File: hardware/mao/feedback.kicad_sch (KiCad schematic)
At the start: 20 parts, among them J501 LRA, Q501 AO3400A, U501 MAX98357AETE+T, U502 DRV2605LDGSR, U503 IRM-H638T/TR2

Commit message: MAO A0 revision: stock Winstar panel through a tail slot, AW9364 backlight, routed 4-layer board
Hardware changes from the verification audits:
- display: stock Winstar WF0128BTYAA4DNN0 (70 mm tail) through a routed slot at 9 o'clock
  to J301 on B.Cu; panel pin k on pad 19-k
- backlight: VLED+ on VSYS into an AW9364 (U303) constant-current sink, 40 mA nominal;
  Q301/R303-R305 removed
- display rail: TPS22919 (SC70-6, 1.1 mm: fits under the panel) with its VIN cap; CT cap gone
- +3V3 at 3.18 V (FB 536k), UVLO filter cap, charger ISET 4.3k (207 mA), /CE from the
  expander with a pull-down, charger moved to F under the panel, SD_MODE series 2.2k
- IR_TX on GPIO38, EXP_RST_N on GPIO39 (MTCK reset pull-up lit the IR LEDs)
- IR receiver and ToF pulled inside the ring lip; M2 boss / screw-head keep-outs

Layout: re-placed and re-routed. DRC 0 violations, 0 unconnected; every plane one piece
(the grid router now undoes any L3 route or via that splits a plane); 192 through vias.
Silk: type scale, 6 x 6 S/N field with the JLC order-number placeholder, 4.6 mm back mark,
references kept off vias, and a few easter eggs (a sleeping cat under the face, boop,
meow, 9 lives, MADE FOR BAD IDEAS).

Checks: ERC 0, silk text 0 findings, enclosure check 0 findings (mech_check.py), all
simulations pass (S3 AW9364, S10 TPS22919, S13 207 mA). Docs: bring-up, factory test,
power budget, architecture, mechanical (tail path), pin map. Firmware: dev command
"mao power charge off|on", self-test pad floor for the 3.18 V rail; merge patch regenerated.

Co-Authored-By: Claude Opus 5.5 <noreply@anthropic.com>
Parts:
- added R507: 2.2k, Resistor_SMD:R_0402_1005Metric, symbol Device:R
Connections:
- net AMP_SD_N: now also R507.1; no longer U501.4 (~{SD_MODE})
- new net AMP_SD: R507.2, U501.4 (~{SD_MODE})
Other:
- note added: "(117)."
- note added: "(datasheet state, deliberate). Speaker:"
- note added: "(datasheet: series R when VDDIO can"
- note added: "MAX98357A I2S class-D from VSYS. SD_MODE"
- note added: "MAX98357A I2S class-D from VSYS. SD_MODE from the expander through 2.2k (datasheet: series R when VDDIO can exceed"
- note added: "Same Sky CMS-150803-088S-X8 (15 x 8 x 3"
- note added: "Sky CMS-150803-088S-X8 (15 x 8 x 3 mm, 8 ohm, 0.8 W) in the base at 9 o'clock; its own spring contacts press on two"
- note added: "V = left channel. GAIN_SLOT open = 9 dB"
- note added: "VDD): low = 0.6 uA shutdown, 3.2 V = left channel. GAIN_SLOT open = 9 dB (datasheet state, deliberate). Speaker: Same"
- note added: "exceed VDD): low = 0.6 uA shutdown, 3.2"
- note added: "from the expander through 2.2k"
- note added: "mm, 8 ohm, 0.8 W) in the base at 9"
- note added: "o'clock; its own spring contacts press"
- note added: "on two pads on B.Cu (LS501)."
- note added: "pads on B.Cu (LS501)."
- note added: "rating at any VSYS up to 4.5 V and any Vf). AO3400A low side, gate pulled down and driven from GPIO38, a pin without a reset pull-up: dark at reset"
- note removed: "9 o'clock; its own spring contacts press on two pads on B.Cu (LS501)."
- note removed: "= 9 dB (datasheet state, deliberate). Speaker: Same Sky CMS-150803-088S-X8 (15 x 8 x 3 mm, 8 ohm, 0.8 W) in the base at"
- note removed: "MAX98357A I2S class-D from VSYS. SD_MODE from the expander: low = 0.6 uA shutdown, 3.3 V = left channel. GAIN_SLOT open"
- note removed: "rating at any VSYS up to 4.5 V and any Vf). AO3400A low side, gate pulled down: dark at reset (117)."
- moved on the sheet: C506, R505, R506, U503

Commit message: MAO A0 schematic: one frame per block, wired local nets, no overprinted names
ODD JOBS audit 2, X8 (rules 187, 188):
- Parts added late (C111, R117, R507) join their block's frame instead of opening a duplicate frame
  with a copy of its note that ran over the neighbours.
- A two-pin part on a net that only joins it to one side pin of its block's IC is wired to that pin
  (the pin's label still names the net, so board, rules and procedures keep their names); feedback and
  UVLO-style dividers hang off their pin as a divider column. Columns step so no wire crosses a part.
- Adjacent pins on one rail share one rail symbol, joined by a wire; a sideways rail symbol keeps its
  name on its own row; turned passives, LEDs and diodes keep their reference and value off the body.
- Rail-source declarations sit in their own frame in the layout flow, not over the title block.
- Two stale notes corrected (C105 distance to VIN, R204 A0 voltage); board fields synced.

ERC 0, DRC 0 / 0 / parity 0.

Co-Authored-By: Claude Opus 5.5 <noreply@anthropic.com>
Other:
- note added: "3.2 V = left channel. GAIN_SLOT open = 9 dB (datasheet state, deliberate). Speaker: Same Sky CMS-150803-088S-X8 (15 x 8 x 3 mm, 8 ohm, 0.8 W) in"
- note added: "65 mA rating at any VSYS up to 4.5 V and any Vf). AO3400A low side, gate pulled down and driven from GPIO38, a pin without a reset"
- note added: "DRV2605L closed-loop LRA driver from VSYS, I2C 0x5A, EN from the expander (4 uA off). IN/TRIG low: playback by"
- note added: "I2C. Pin 6 VDD/NC left open (SLOS854D: optional supply, tie to VDD or float). LRA LD0832AA (235 Hz, 1.8 Vrms)"
- note added: "IRM-H638T (as LCDkit), top-view, looking up through the window border. Powered from expander"
- note added: "MAX98357A I2S class-D from VSYS. SD_MODE from the expander through 2.2k (datasheet: series R when VDDIO can exceed VDD): low = 0.6 uA shutdown,"
- note added: "P5 through 100R/4.7 uF only when listening (0.4 mA). OUT pull-up goes to the switched"
- note added: "RAIL SOURCES"
- note added: "Two side-emitting 940 nm LEDs at the back edge (B.Cu), each with its own 56R from VSYS (26-59 mA pulses at 38 kHz, 33 % duty: under the"
- note added: "defined low while it is off."
- note added: "glued to the base, leads to J501."
- note added: "pull-up: dark at reset (117)."
- note added: "supply, never to +3V3, so an unpowered receiver is never back-powered and GPIO40 reads a"
- note added: "the base at 9 o'clock; its own spring contacts press on two pads on B.Cu (LS501)."
- note removed: "(117)."
- note removed: "(datasheet state, deliberate). Speaker:"
- note removed: "(datasheet: series R when VDDIO can"
- note removed: "DRV2605L closed-loop LRA driver from VSYS, I2C 0x5A, EN from the expander (4 uA off). IN/TRIG low: playback by I2C."
- note removed: "GPIO40 reads a defined low while it is off."
- note removed: "IRM-H638T (as LCDkit), top-view, looking up through the window border. Powered from"
- note removed: "MAX98357A I2S class-D from VSYS. SD_MODE"
- note removed: "MAX98357A I2S class-D from VSYS. SD_MODE from the expander through 2.2k (datasheet: series R when VDDIO can exceed"
- note removed: "Pin 6 VDD/NC left open (SLOS854D: optional supply, tie to VDD or float). LRA LD0832AA (235 Hz, 1.8 Vrms) glued to"
- note removed: "RAIL SOURCE DECLARATIONS"
- note removed: "Same Sky CMS-150803-088S-X8 (15 x 8 x 3"
- note removed: "Sky CMS-150803-088S-X8 (15 x 8 x 3 mm, 8 ohm, 0.8 W) in the base at 9 o'clock; its own spring contacts press on two"
- note removed: "Two side-emitting 940 nm LEDs at the back edge (B.Cu), each with its own 56R from VSYS (26-59 mA pulses at 38 kHz, 33 % duty: under the 65 mA"
- note removed: "V = left channel. GAIN_SLOT open = 9 dB"
- note removed: "VDD): low = 0.6 uA shutdown, 3.2 V = left channel. GAIN_SLOT open = 9 dB (datasheet state, deliberate). Speaker: Same"
- note removed: "exceed VDD): low = 0.6 uA shutdown, 3.2"
- note removed: "expander P5 through 100R/4.7 uF only when listening (0.4 mA). OUT pull-up goes to the"
- note removed: "from the expander through 2.2k"
- note removed: "mm, 8 ohm, 0.8 W) in the base at 9"
- note removed: "o'clock; its own spring contacts press"
- note removed: "on two pads on B.Cu (LS501)."
- note removed: "pads on B.Cu (LS501)."
- note removed: "rating at any VSYS up to 4.5 V and any Vf). AO3400A low side, gate pulled down and driven from GPIO38, a pin without a reset pull-up: dark at reset"
- note removed: "switched supply, never to +3V3, so an unpowered receiver is never back-powered and"
- note removed: "the base, leads to J501."
- moved on the sheet: C501, C502, C503, C504, C505, C506, D501, D502, J501, LS501, Q501, R501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

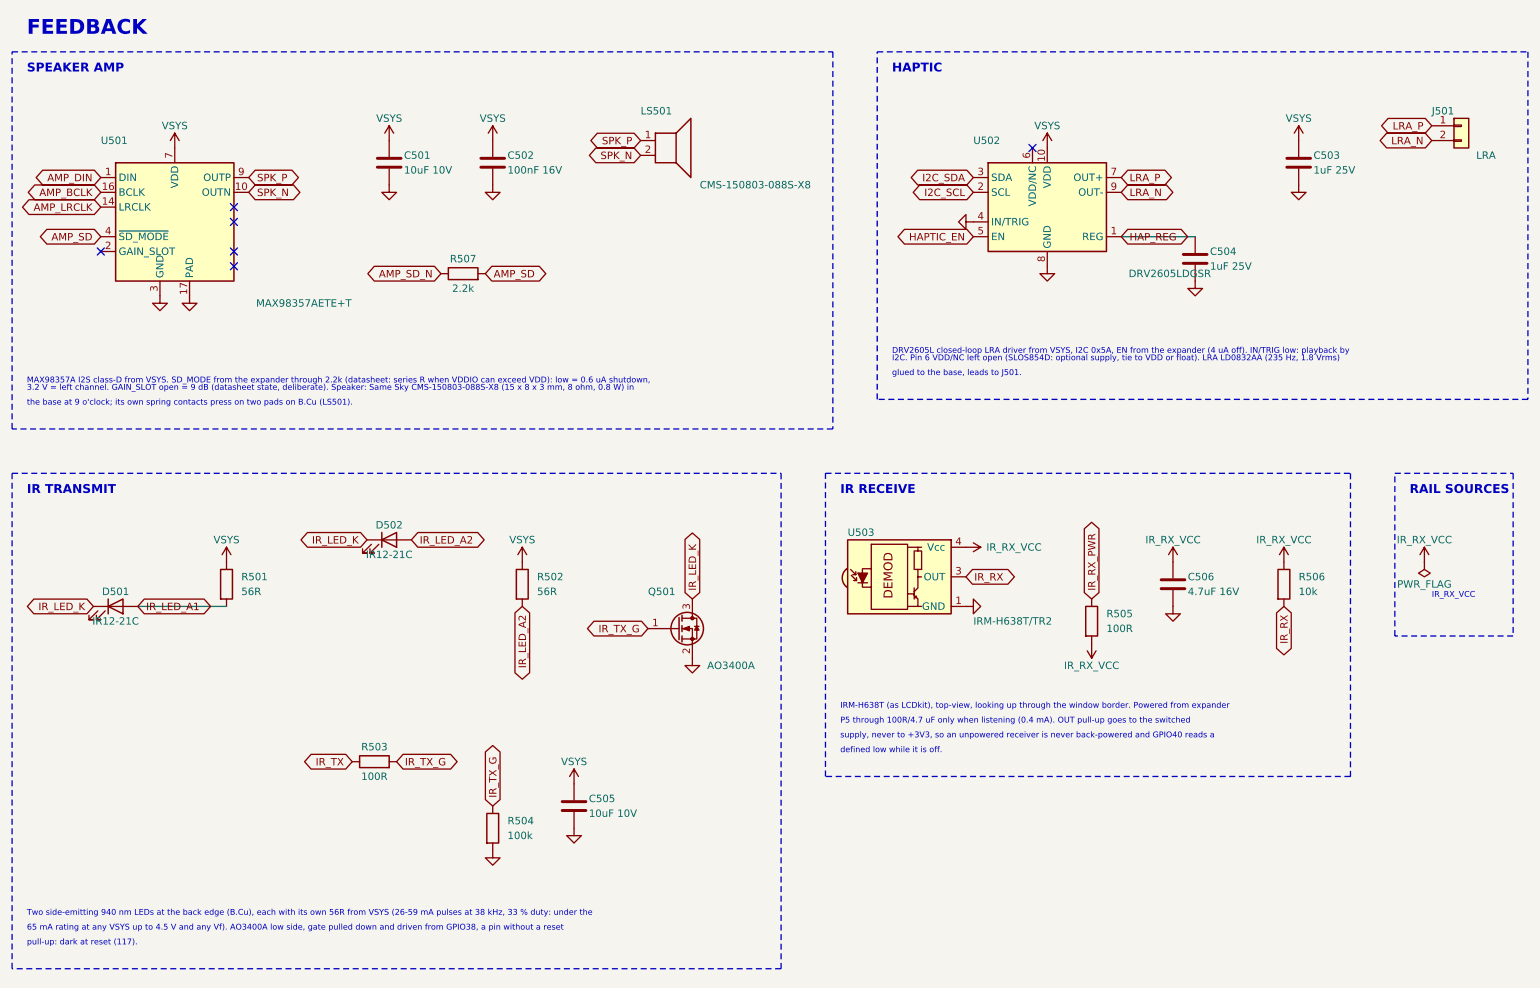
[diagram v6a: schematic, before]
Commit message: MAO A0 audit 3 fixes: VSYS feed un-necked, speaker lines over VSYS, silk leaders to their parts
Electrical audit 3 (no blocker; issue I-1):
- 11 o'clock panel tab 320 -> 328 deg: its keep-out necked the L3 VSYS band to 0.27 mm beside H1
- via-free corner where the VSYS branch turns into the backlight bar (a C205/U202 via left 0.26 mm)
- plane_check: GND and rail regions refilled at 0.5 mm minimum width must not split (necks fail
  the build); the +3V3 mesh is reported
- self-test board_id upper limit 1700 -> 1720 mV (the 3.32 V rail corner reached 1.697 V)
- comments: rail 3.10-3.32 V, AW9364 dropout, TPS22919 turn-on vs rise, panel clock, Kconfig help
- D101 drawn as a unidirectional TVS (zener glyph); module +3V3 via on C202's branch axis

ODD JOBS audit 3 (0 FAIL; recommended fixes):
- VSYS branch extended under both speaker lines (they sat over the VSYS/+3V3 zone gap); LCD_RST_N
  off L3; L3/L4 broadside 17.4 -> 13.8 mm
- EXP_RST_N's leg to TP11 designed on L3 (left to the router it detoured)
- leaders end 0.3 mm off their own part, at least 0.1 mm nearer it than any other part
- no silk text on touch-electrode copper (silk.py, mao_labels.py, check_silk_text.py): REAR and
  MIC moved
- schematic note lines on a 2.54 mm pitch (snapped 2.29 mm printed pairs that touched); tail note
- back identity on a reserved via-free spot; RSSI check with and without the LRA; drawing text
- final board: DRC 0/0/0, planes whole, no rail neck under 0.5 mm, silk 83 texts 0 findings,
  mech 0, 205 vias, 921 segments on 45 degrees; firmware 5 builds 0 warnings, 240 host checks;
  merge patch re-verified on b17187e

Co-Authored-By: Claude Opus 5.5 <noreply@anthropic.com>
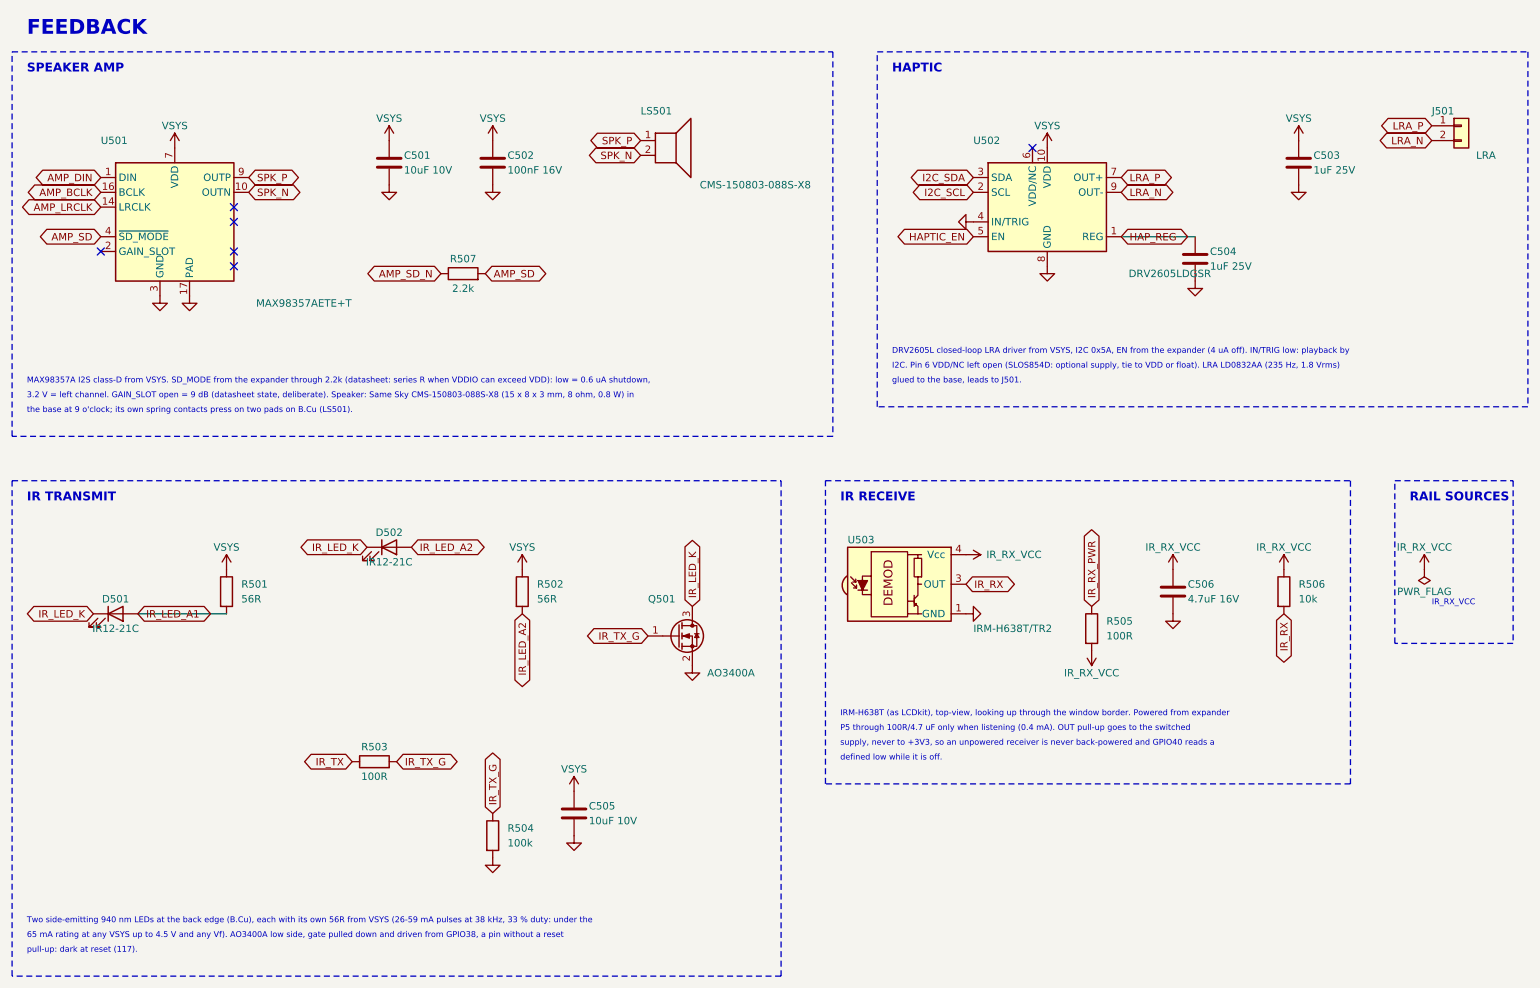
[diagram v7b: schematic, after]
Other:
- moved on the sheet: C505, C506, D501, D502, Q501, R501, R502, R504, R505, R506, U503

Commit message: A1 capture: Gate C architecture on the A0 puck (schematic, ERC 0)
circuit.py now describes MAO_MAIN A1 (ERC 0 at all severities, 137 parts, 75 nets):
- ESP32-S3-MINI-1-N8 on RF_Module:ESP32-S2-MINI-1 (Gate C land audit); GPIO0 = BOOT pad only
  (10k + TP8), GPIO3/45/46 NC, 22R + DNP 10 pF on USB at the module, VBUS_SENSE 100k/150k.
- BQ25185 (ILIM/VSET 18k: 4.2 V / 500 mA; ISET 1.43k: 210 mA as A0; TS/MR to the NTC, DNP 10k,
  TSMR pad; /CE 100k pull-down; STAT1/2 10k to +3V3) replaces BQ24073.
- TPS62840 (VSET 102k = 3.2 V, SLVSEC6D table 1; 2.2 uH, CIN 4.7 uF, COUT 10 uF; MODE/STOP low,
  EN to VIN) replaces TPS63802 and its UVLO/FB dividers; LINK_REG 0R added, LINK_BAT kept.
- ICM-42670-P replaces LSM6DSOX on the same land (0x68, INT1 100k pull-up, INT2 not wired).
- DRV2605L VDD and pin 6 on +3V3; constant-current backlight sink (TLV9061 + DMG2302UK, 3.3R)
  replaces the AW9364; TPS22916C for the panel rail and the IR receiver rail.
- MAX98357A SD_MODE straight from GPIO9 (2.2k series dropped: +3V3 <= VSYS by topology).
- Removed: touch (4 zones, electrodes, springs), SPH0641, OPT3004, TCA6408A, board-ID divider.
- I2C pull-ups 4.7k; new fixture pads BL, AMP, TE, PRS, HLA, TSMR, CE, IO21, IO26.
- Battery connector stays JST SH: the Gate C JST PH side entry is 4.8 mm tall (KiCad STEP of the
  PH side-entry housing) against the 3.2 mm B-side zone over the cell; owner decision.
Parts kept from A0 keep their references; removed numbers are retired.
New footprint MAO:TI_DLC0008B_VSON-HR-8 (TI land example 4224310/A, from the Gate C generator);
A0-only custom footprints removed. Board name MAO_MAIN_A1; A0 board/outputs removed from this tree
(they stay on the A0 branch).

Co-Authored-By: Claude Opus 5.5 <noreply@anthropic.com>
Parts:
- removed R507: 2.2k, Resistor_SMD:R_0402_1005Metric, symbol Device:R
- added C508: 1uF 25V, Capacitor_SMD:C_0402_1005Metric, symbol Device:C
- added U504: TPS22916CYFPR, Package_BGA:Texas_PicoStar_BGA-4_0.758x0.758mm_Layout2x2_P0.4mm, symbol MAO:TPS22916C
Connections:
- net GND: now also C508.2, U504.B1 (GND)
- net VSYS: no longer C503.1, U502.10 (VDD)
- net +3V3: now reaches U502.6 (VDD/NC)
- net +3V3: now also C503.1, U502.10 (VDD), C508.1, U504.A2 (VIN)
- net IR_RX_PWR renamed AUX_3V3
- net AUX_3V3: now also U504.A1 (VOUT)
- new net AUX_PWR_EN: U504.B2 (ON)
- no-connect marks 6 -> 5
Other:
- note added: "65 mA rating at any VSYS up to 4.5 V and any Vf). AO3400A low side driven from GPIO17 through 100R; the 100k at the gate is also IR_TX's"
- note added: "AUX_PWR_EN (GPIO16), through 100R/4.7 uF only while listening (0.4 mA). OUT pull-up goes to the switched supply, never to +3V3, so an unpowered"
- note added: "DRV2605L closed-loop LRA driver on +3V3 (Gate C: its SDA/SCL/EN/TRIG absolute maximum is VDD + 0.3 V, so it"
- note added: "I2C 0x5A, EN from GPIO14 with 100k pull-down (4 uA off). IN/TRIG low: playback by I2C. REG 1 uF, VDD 1 uF. LRA"
- note added: "IRM-H638T (as LCDkit), top-view, looking up through the window border, on GPIO36. Powered from AUX_3V3, a TPS22916C on +3V3 switched by"
- note added: "LD0832AA (235 Hz, 1.8 Vrms) glued to the base, leads to J501."
- note added: "MAX98357A I2S class-D from VSYS (Gate C). SD_MODE driven directly from GPIO9 (AMP_SD): high = left channel, low = 0.6 uA shutdown; 100k pull-down"
- note added: "occur, +3V3 <= VSYS by topology. I2S on GPIO40/41/42. GAIN_SLOT open = 9 dB. Speaker: Same Sky CMS-150803-088S-X8 (15 x 8 x 3 mm, 8 ohm, 0.8 W) in"
- note added: "plus the internal 100k: silent from reset (ODD JOBS 116). A0's 2.2k series resistor is gone: its datasheet reason (logic high above VDD) cannot"
- note added: "pull-down: dark at reset (117)."
- note added: "receiver is never back-powered and reads a defined low while it is off."
- note added: "shares the always-on rail of the I2C pull-ups and is never supply-gated). VDD pin 10 and VDD/NC pin 6 to +3V3."
- note removed: "3.2 V = left channel. GAIN_SLOT open = 9 dB (datasheet state, deliberate). Speaker: Same Sky CMS-150803-088S-X8 (15 x 8 x 3 mm, 8 ohm, 0.8 W) in"
- note removed: "65 mA rating at any VSYS up to 4.5 V and any Vf). AO3400A low side, gate pulled down and driven from GPIO38, a pin without a reset"
- note removed: "DRV2605L closed-loop LRA driver from VSYS, I2C 0x5A, EN from the expander (4 uA off). IN/TRIG low: playback by"
- note removed: "I2C. Pin 6 VDD/NC left open (SLOS854D: optional supply, tie to VDD or float). LRA LD0832AA (235 Hz, 1.8 Vrms)"
- note removed: "IRM-H638T (as LCDkit), top-view, looking up through the window border. Powered from expander"
- note removed: "MAX98357A I2S class-D from VSYS. SD_MODE from the expander through 2.2k (datasheet: series R when VDDIO can exceed VDD): low = 0.6 uA shutdown,"
- note removed: "P5 through 100R/4.7 uF only when listening (0.4 mA). OUT pull-up goes to the switched"
- note removed: "defined low while it is off."
- note removed: "glued to the base, leads to J501."
- note removed: "pull-up: dark at reset (117)."
- note removed: "supply, never to +3V3, so an unpowered receiver is never back-powered and GPIO40 reads a"
- title: MAO_MAIN A0 - Feedback -> MAO_MAIN A1 - Feedback
- moved on the sheet: C505, C506, D501, D502, Q501, R501, R502, R503, R504, R505, R506, U503
